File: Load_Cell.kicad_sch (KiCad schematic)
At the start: 1 part, among them J3 Conn_01x04

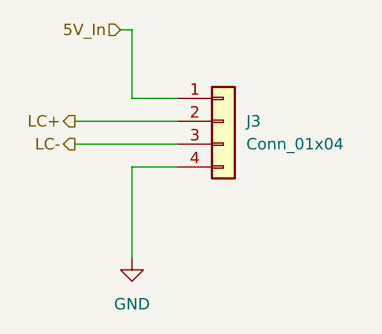
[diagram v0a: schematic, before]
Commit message: Updated to 4-pin fans, moved power pages together, deleted old reference.
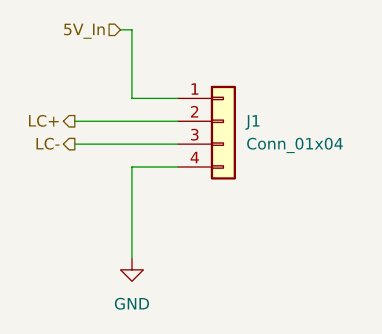
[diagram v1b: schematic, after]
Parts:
- J1: renamed from J3; footprint (none) -> Connector_JST:JST_EH_B4B-EH-A_1x04_P2.50mm_Vertical
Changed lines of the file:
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@@
 		(dnp no)
 		(fields_autoplaced yes)
-		(property "Reference" "#PWR022"
+		(property "Reference" "#PWR0115"
 			(at 165.1 106.68 0)
 			(effects
@@
 			(project ""
 				(path "/24817451-dfe0-4b9a-9d93-7304529c9d58/3fe78498-f3da-4a4e-905d-c6815bbc6a4f"
-					(reference "#PWR022")
+					(reference "#PWR0115")
 					(unit 1)
 				)
@@
 		(dnp no)
 		(fields_autoplaced yes)
-		(property "Reference" "J3"
+		(property "Reference" "J1"
 			(at 177.8 85.0899 0)
 			(effects
@@
 			)
 		)
-		(property "Footprint" ""
+		(property "Footprint" "Connector_JST:JST_EH_B4B-EH-A_1x04_P2.50mm_Vertical"
 			(at 175.26 85.09 0)
 			(effects
@@
 			(project ""
 				(path "/24817451-dfe0-4b9a-9d93-7304529c9d58/3fe78498-f3da-4a4e-905d-c6815bbc6a4f"
-					(reference "J3")
+					(reference "J1")
 					(unit 1)
 				)
